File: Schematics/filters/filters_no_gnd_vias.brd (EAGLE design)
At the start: 100.6 x 44.8 mm, 102 parts, among them IC1 NE5532N, IC2 NE5532N, IC3 NE5532N, IC4 NE5532N, IC5 NE5532N, IC6 NE5532N, IC7 NE5532N, J1 3_PIN_AMPCONN, J2 3_PIN_AMPCONN, J3 3_PIN_AMPCONN

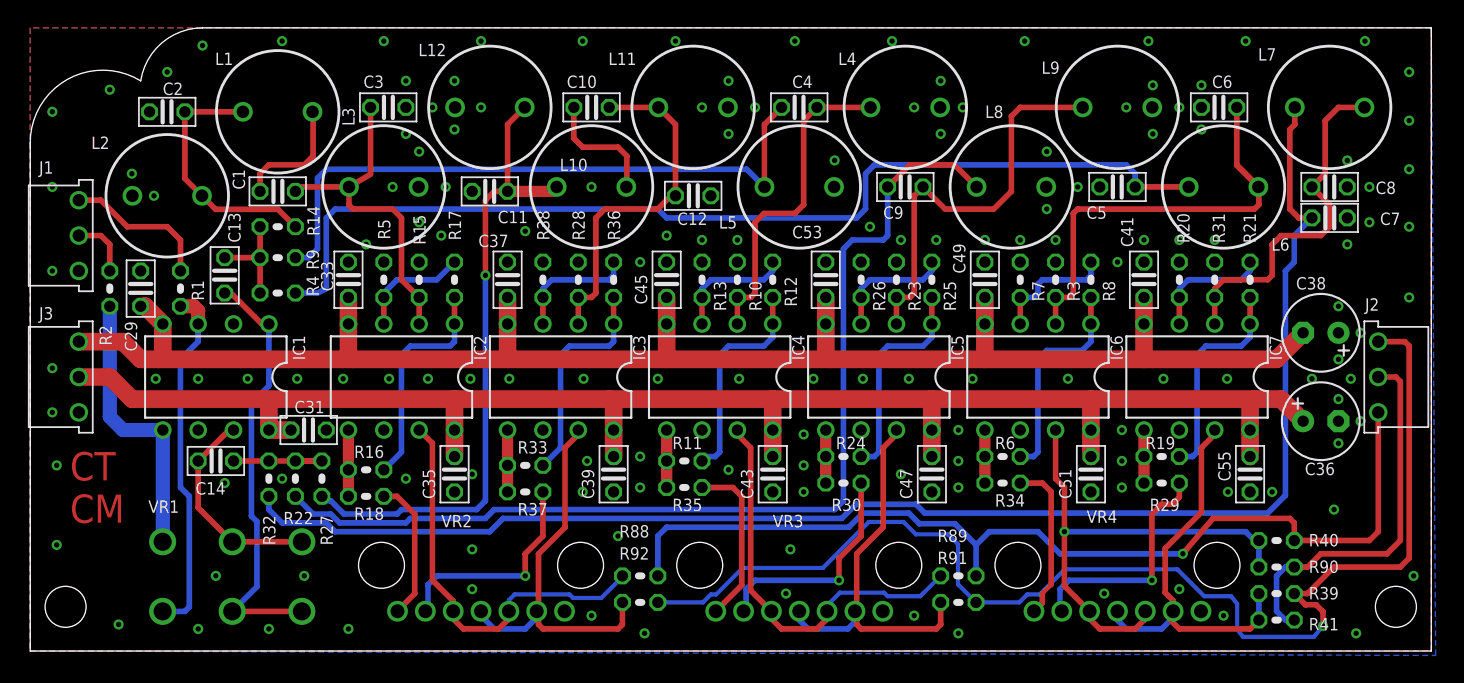
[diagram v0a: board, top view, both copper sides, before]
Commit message: updated filter board. changed cap footprint
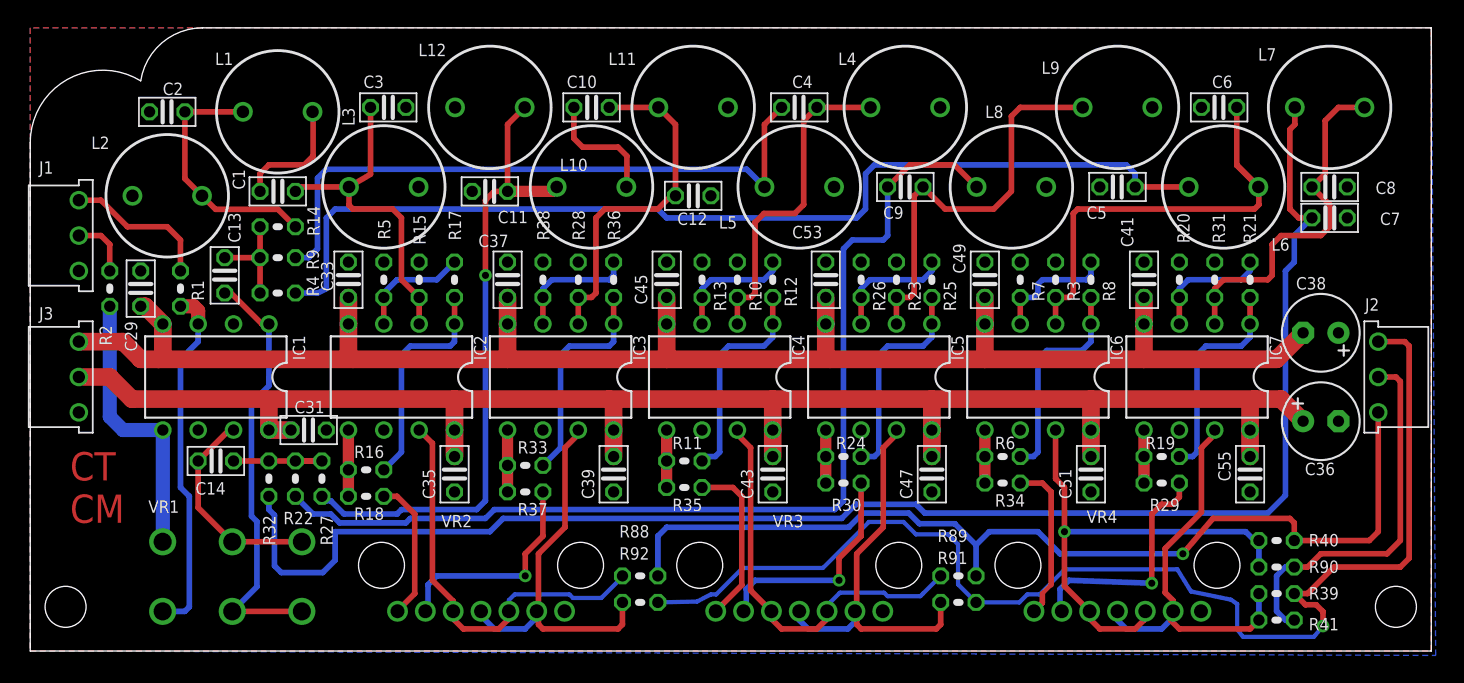
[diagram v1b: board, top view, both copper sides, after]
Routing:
- net N$44: track 106.3 -> 112.0 mm
